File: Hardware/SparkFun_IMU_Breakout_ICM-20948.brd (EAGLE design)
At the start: 25.4 x 25.4 mm, 79 parts, among them U1 TXB0108DQSR, U2 9DoF IMU, U3 1.8V/100mA

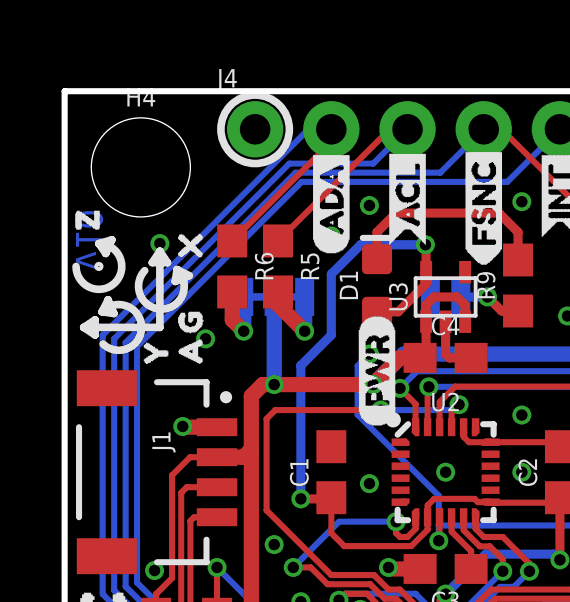
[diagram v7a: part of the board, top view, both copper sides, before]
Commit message: Reposition axis labels
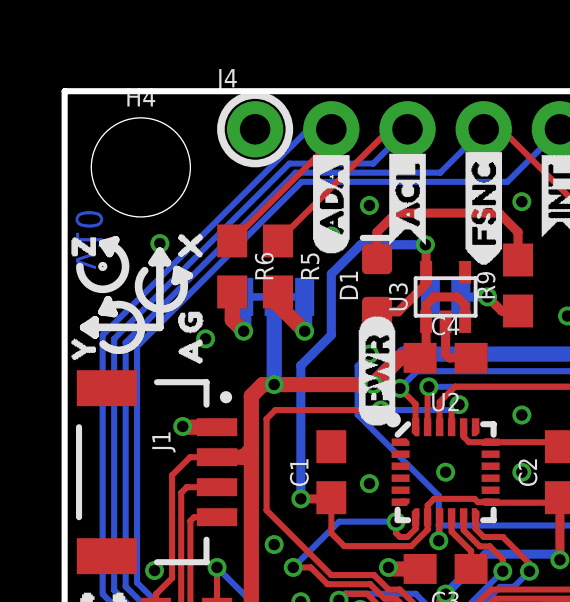
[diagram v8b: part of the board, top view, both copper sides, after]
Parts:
- moved U$35 2.42 mm to (0.64, 15.7)
- moved U$36 0.90 mm to (0.64, 19.2)
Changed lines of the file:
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@@
 <layer number="21" name="tPlace" color="16" fill="1" visible="yes" active="yes"/>
 <layer number="22" name="bPlace" color="14" fill="1" visible="yes" active="yes"/>
-<layer number="23" name="tOrigins" color="15" fill="1" visible="no" active="yes"/>
+<layer number="23" name="tOrigins" color="15" fill="1" visible="yes" active="yes"/>
 <layer number="24" name="bOrigins" color="15" fill="1" visible="no" active="yes"/>
 <layer number="25" name="tNames" color="7" fill="1" visible="no" active="yes"/>
@@
 <dimension x1="0" y1="25.4" x2="25.4" y2="25.4" x3="12.7" y3="33.02" textsize="1.778" textratio="15" layer="47" unit="inch"/>
 <dimension x1="0" y1="25.4" x2="0" y2="0" x3="-7.62" y3="12.7" textsize="1.778" textratio="15" layer="47" unit="inch"/>
-<circle x="1.143" y="19.558" radius="0.0635" width="0.1778" layer="21"/>
-<wire x1="1.143" y1="20.32" x2="0.381" y2="19.558" width="0.254" layer="21" curve="-270"/>
-<wire x1="1.143" y1="20.32" x2="1.3716" y2="19.9898" width="0.254" layer="21"/>
-<wire x1="1.3716" y1="19.9898" x2="1.5748" y2="20.447" width="0.254" layer="21"/>
-<wire x1="1.5748" y1="20.447" x2="1.143" y2="20.32" width="0.254" layer="21"/>
-<wire x1="1.27" y1="20.193" x2="1.27" y2="20.32" width="0.127" layer="21"/>
-<wire x1="1.3716" y1="20.2184" x2="1.4732" y2="20.2946" width="0.254" layer="21"/>
+<circle x="1.27" y="19.558" radius="0.0635" width="0.1778" layer="21"/>
+<wire x1="1.27" y1="20.32" x2="0.508" y2="19.558" width="0.254" layer="21" curve="-270"/>
+<wire x1="1.27" y1="20.32" x2="1.4986" y2="19.9898" width="0.254" layer="21"/>
+<wire x1="1.4986" y1="19.9898" x2="1.7018" y2="20.447" width="0.254" layer="21"/>
+<wire x1="1.7018" y1="20.447" x2="1.27" y2="20.32" width="0.254" layer="21"/>
+<wire x1="1.397" y1="20.193" x2="1.397" y2="20.32" width="0.127" layer="21"/>
+<wire x1="1.4986" y1="20.2184" x2="1.6002" y2="20.2946" width="0.254" layer="21"/>
 <wire x1="3.746453125" y1="19.453984375" x2="2.669415625" y2="19.41825625" width="0.254" layer="21" curve="-270"/>
 <wire x1="3.746453125" y1="19.453984375" x2="3.68775" y2="19.056690625" width="0.254" layer="21"/>
@@
 <element name="U$33" library="buzzard_labels (1)" package="PWR0" value="" x="10.414" y="14.1986" rot="R90"/>
 <element name="U$34" library="buzzard_labels (1)" package="X0" value="" x="4.191" y="19.177" rot="R90"/>
-<element name="U$35" library="buzzard_labels (1)" package="Y1" value="" x="3.048" y="15.621" rot="R90"/>
-<element name="U$36" library="buzzard_labels (1)" package="Z2" value="" x="0.762" y="20.066" rot="R90"/>
+<element name="U$35" library="buzzard_labels (1)" package="Y1" value="" x="0.635" y="15.748" rot="R90"/>
+<element name="U$36" library="buzzard_labels (1)" package="Z2" value="" x="0.635" y="19.177" rot="R90"/>
 <element name="U$37" library="buzzard_labels (1)" package="G5" value="" x="4.191" y="16.637" rot="R90"/>
 <element name="U$38" library="buzzard_labels (1)" package="A4" value="" x="4.191" y="15.621" rot="R90"/>
